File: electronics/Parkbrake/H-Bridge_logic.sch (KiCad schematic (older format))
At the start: 20 parts, among them U1 CD74HC03M, U2 74LV08D, U3 CD74HC03M, U4 74LV08D

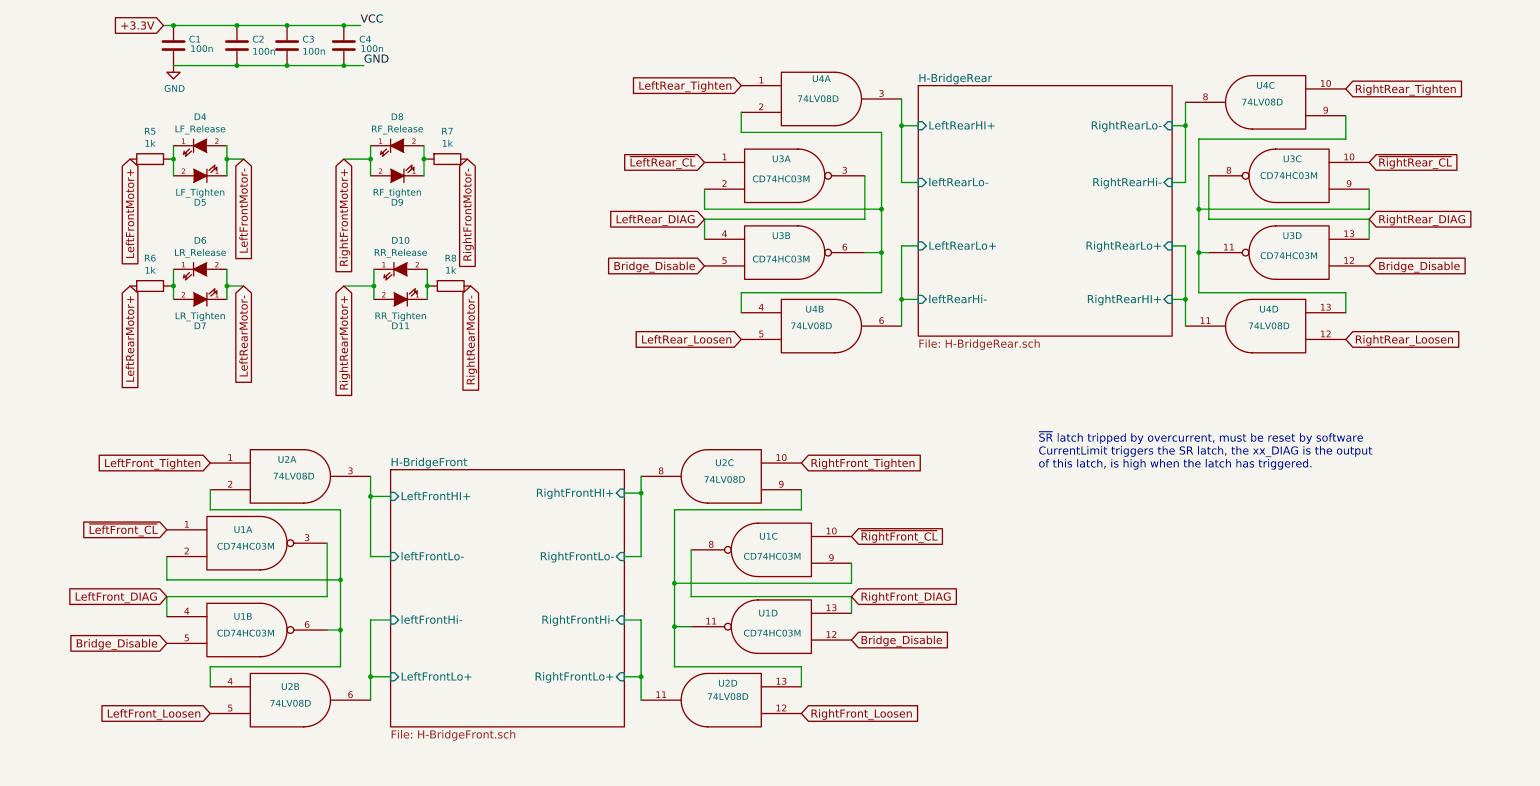
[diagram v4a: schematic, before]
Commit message: More fixes and chenged components eat less boardspace
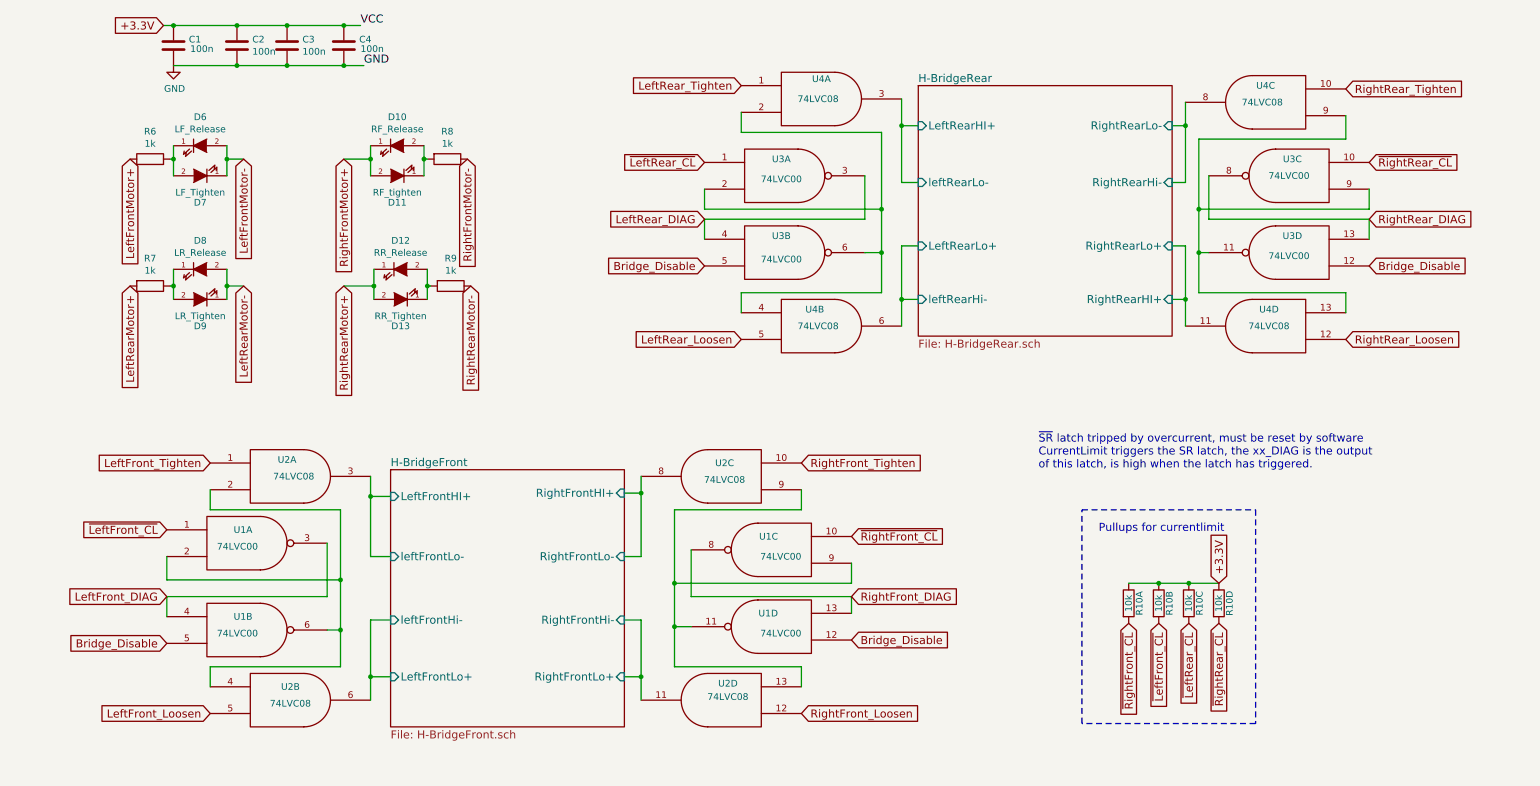
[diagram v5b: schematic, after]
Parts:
- added R10: 10k, Resistors_SMD:R_Array_Concave_4x0603, symbol Rnet4
- U1, U3: value CD74HC03M -> 74LVC00; footprint (none) -> Housings_SSOP:TSSOP-14_4.4x5mm_Pitch0.65mm; farnell 1749880 -> 2438786; part CD74HC03M -> 74LVC00APW.118
- U1: value CD74HC03M -> 74LVC00; part CD74HC03M -> (none)
- U1: value CD74HC03M -> 74LVC00
- U2, U4: value 74LV08D -> 74LVC08; footprint (none) -> Housings_SSOP:TSSOP-14_4.4x5mm_Pitch0.65mm; farnell 1085354 -> 2445097; part 74LV08D -> 74LVC08APW-Q100.11
- U2, U4: value 74LV08D -> 74LVC08
- U3: value CD74HC03M -> 74LVC00; part CD74HC03M -> SN74HC03PW
- renumbered D8 to D10, D9 to D11, D10 to D12, D11 to D13, D4 to D6, D5 to D7, D6 to D8, D7 to D9, R5 to R6, R6 to R7, R7 to R8, R8 to R9
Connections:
- net VCC: now also R10.1, R10.2, R10.3, R10.4
- net ~LeftFront_CL: now also R10.7
- net ~LeftRear_CL: now also R10.6
- net ~RightFront_CL: now also R10.8
- net ~RightRear_CL: now also R10.5
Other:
- note added: "Pullups for currentlimit"

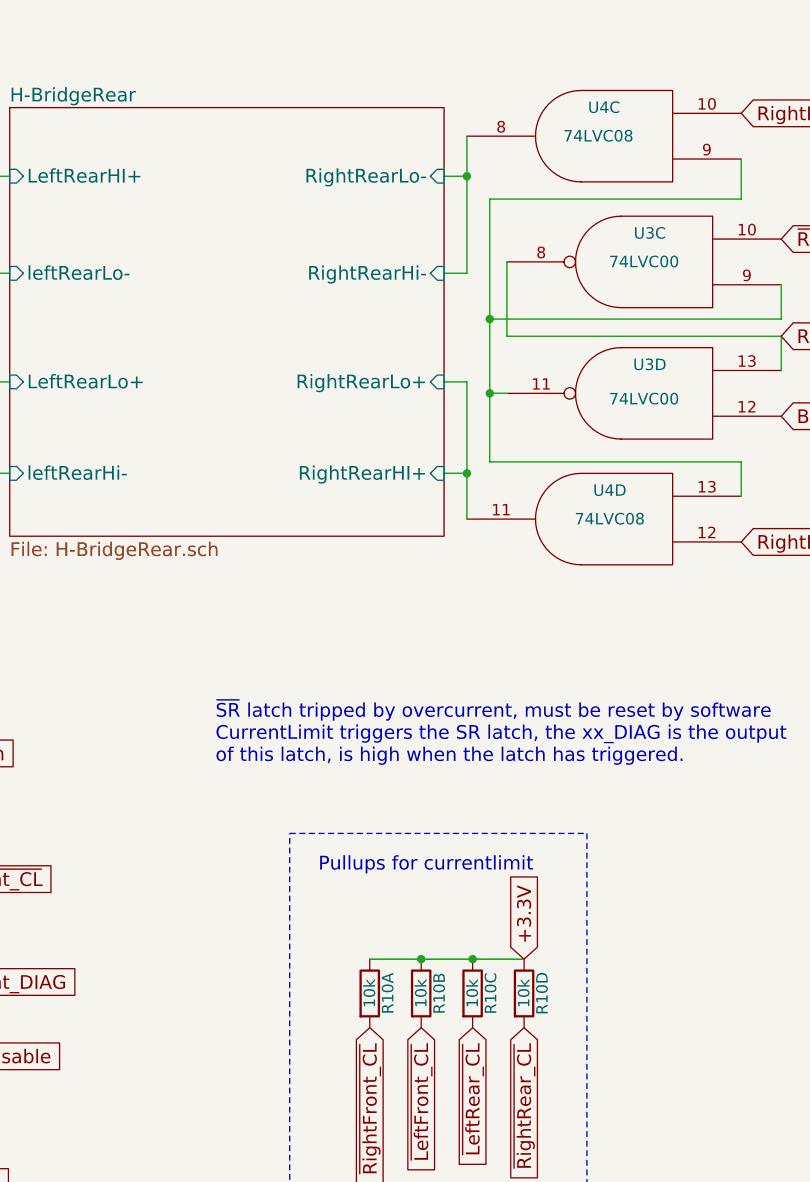
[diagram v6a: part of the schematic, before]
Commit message: more work on parkbrake ecu Rear H-bridge more or less finished
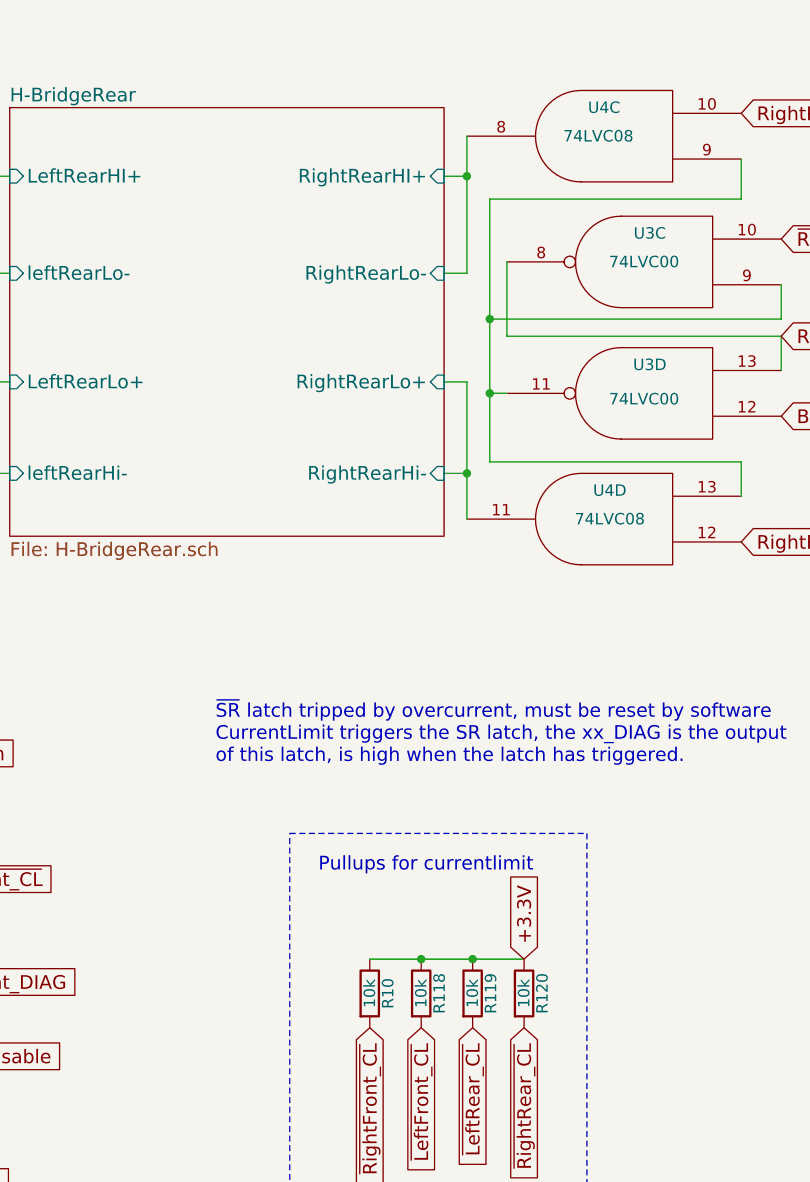
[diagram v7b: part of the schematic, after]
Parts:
- removed R10: 10k, Resistors_SMD:R_Array_Concave_4x0603, symbol Rnet4
- added R10, R118, R119, R120: 10k, Resistors_SMD:R_0805, symbol R
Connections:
- net H-BridgeRear/RightRearHI+: now also U4.8; no longer U4.11
- net H-BridgeRear/RightRearHi-: now also U4.11; no longer U4.8
- net VCC: now also R10.1, R118.1, R119.1, R120.1
- net ~LeftFront_CL: now also R118.2
- net ~LeftRear_CL: now also R119.2
- net ~RightFront_CL: now also R10.2
- net ~RightRear_CL: now also R120.2
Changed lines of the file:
@@
 F4 "leftRearHi-" I L 7000 2950 60
 F5 "leftRearLo-" I L 7000 2075 60
-F6 "RightRearHI+" I R 8900 2950 60
+F6 "RightRearLo-" I R 8900 2075 60
 F7 "RightRearLo+" I R 8900 2550 60
-F8 "RightRearHi-" I R 8900 2075 60
-F9 "RightRearLo-" I R 8900 1650 60
+F8 "RightRearHI+" I R 8900 1650 60
+F9 "RightRearHi-" I R 8900 2950 60
 $EndSheet
 $Comp
@@
 $EndComp
 $Comp
-L GND #PWR019
+L GND #PWR10
 U 1 1 5706E47E
 P 1425 1200
-F 0 "#PWR019" H 1425 950 50  0001 C CNN
+F 0 "#PWR10" H 1425 950 50  0001 C CNN
 F 1 "GND" H 1433 1027 50  0000 C CNN
 F 2 "" H 1425 1200 50  0000 C CNN
@@
 Text GLabel 10375 2350 2    60   Input ~ 0
 RightRear_DIAG
-$Comp
-L Rnet4 R10
-U 1 1 5796B54F
-P 8575 5225
-F 0 "R10" H 8575 5305 50  0000 C CNN
-F 1 "10k" H 8575 5225 50  0000 C CNN
-F 2 "Resistors_SMD:R_Array_Concave_4x0603" H 8575 5155 50  0001 C CNN
-F 3 "" V 8575 5225 50  0000 C CNN
-F 4 "EXB38V103JV" H 8575 5225 60  0001 C CNN "part"
-F 5 "2060107" H 8575 5225 60  0001 C CNN "farnell"
-	1    8575 5225
-	0    1    1    0
-$EndComp
-$Comp
-L Rnet4 R10
-U 2 1 5796B8CA
-P 8800 5225
-F 0 "R10" H 8800 5305 50  0000 C CNN
-F 1 "10k" H 8800 5225 50  0000 C CNN
-F 2 "" H 8800 5155 50  0000 C CNN
-F 3 "" V 8800 5225 50  0000 C CNN
-	2    8800 5225
-	0    1    1    0
-$EndComp
-$Comp
-L Rnet4 R10
-U 3 1 5796B987
-P 9025 5225
-F 0 "R10" H 9025 5305 50  0000 C CNN
-F 1 "10k" H 9025 5225 50  0000 C CNN
-F 2 "" H 9025 5155 50  0000 C CNN
-F 3 "" V 9025 5225 50  0000 C CNN
-	3    9025 5225
-	0    1    1    0
-$EndComp
-$Comp
-L Rnet4 R10
-U 4 1 5796BA4A
-P 9250 5225
-F 0 "R10" H 9250 5305 50  0000 C CNN
-F 1 "10k" H 9250 5225 50  0000 C CNN
-F 2 "" H 9250 5155 50  0000 C CNN
-F 3 "" V 9250 5225 50  0000 C CNN
-	4    9250 5225
-	0    1    1    0
-$EndComp
 Text GLabel 9250 5075 1    60   Input ~ 0
 +3.3V
@@
 Wire Notes Line
 	8225 6125 8225 4525
+$Comp
+L R R10
+U 1 1 579BFFE0
+P 8575 5225
+F 0 "R10" V 8655 5225 50  0000 C CNN
+F 1 "10k" V 8575 5225 50  0000 C CNN
+F 2 "Resistors_SMD:R_0805" V 8505 5225 50  0001 C CNN
+F 3 "" H 8575 5225 50  0000 C CNN
+F 4 "9332391" V 8575 5225 60  0001 C CNN "farnell"
+F 5 "MC01W0805110K" V 8575 5225 60  0001 C CNN "part"
+	1    8575 5225
+	1    0    0    -1
+$EndComp
+$Comp
+L R R118
+U 1 1 579C0194
+P 8800 5225
+F 0 "R118" V 8880 5225 50  0000 C CNN
+F 1 "10k" V 8800 5225 50  0000 C CNN
+F 2 "Resistors_SMD:R_0805" V 8730 5225 50  0001 C CNN
+F 3 "" H 8800 5225 50  0000 C CNN
+F 4 "9332391" V 8800 5225 60  0001 C CNN "farnell"
+F 5 "MC01W0805110K" V 8800 5225 60  0001 C CNN "part"
+	1    8800 5225
+	1    0    0    -1
+$EndComp
+$Comp
+L R R119
+U 1 1 579C029F
+P 9025 5225
+F 0 "R119" V 9105 5225 50  0000 C CNN
+F 1 "10k" V 9025 5225 50  0000 C CNN
+F 2 "Resistors_SMD:R_0805" V 8955 5225 50  0001 C CNN
+F 3 "" H 9025 5225 50  0000 C CNN
+F 4 "9332391" V 9025 5225 60  0001 C CNN "farnell"
+F 5 "MC01W0805110K" V 9025 5225 60  0001 C CNN "part"
+	1    9025 5225
+	1    0    0    -1
+$EndComp
+$Comp
+L R R120
+U 1 1 579C0368
+P 9250 5225
+F 0 "R120" V 9330 5225 50  0000 C CNN
+F 1 "10k" V 9250 5225 50  0000 C CNN
+F 2 "Resistors_SMD:R_0805" V 9180 5225 50  0001 C CNN
+F 3 "" H 9250 5225 50  0000 C CNN
+F 4 "9332391" V 9250 5225 60  0001 C CNN "farnell"
+F 5 "MC01W0805110K" V 9250 5225 60  0001 C CNN "part"
+	1    9250 5225
+	1    0    0    -1
+$EndComp
 $EndSCHEMATC
